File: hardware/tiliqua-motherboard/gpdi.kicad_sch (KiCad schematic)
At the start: 18 parts, among them J10 DVI_GPDI_D_1.4, U3 PCA9306DP

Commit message: big HDMI
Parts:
- J10: footprint Connector_Video:HDMI_Micro-D_Molex_46765-1x01 -> Connector_Video:HDMI_A_Amphenol_10029449-x01xLF_Horizontal
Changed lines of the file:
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@@
 			)
 		)
-		(property "Footprint" "Connector_Video:HDMI_Micro-D_Molex_46765-1x01"
+		(property "Footprint" "Connector_Video:HDMI_A_Amphenol_10029449-x01xLF_Horizontal"
 			(at 172.085 91.44 0)
 			(effects

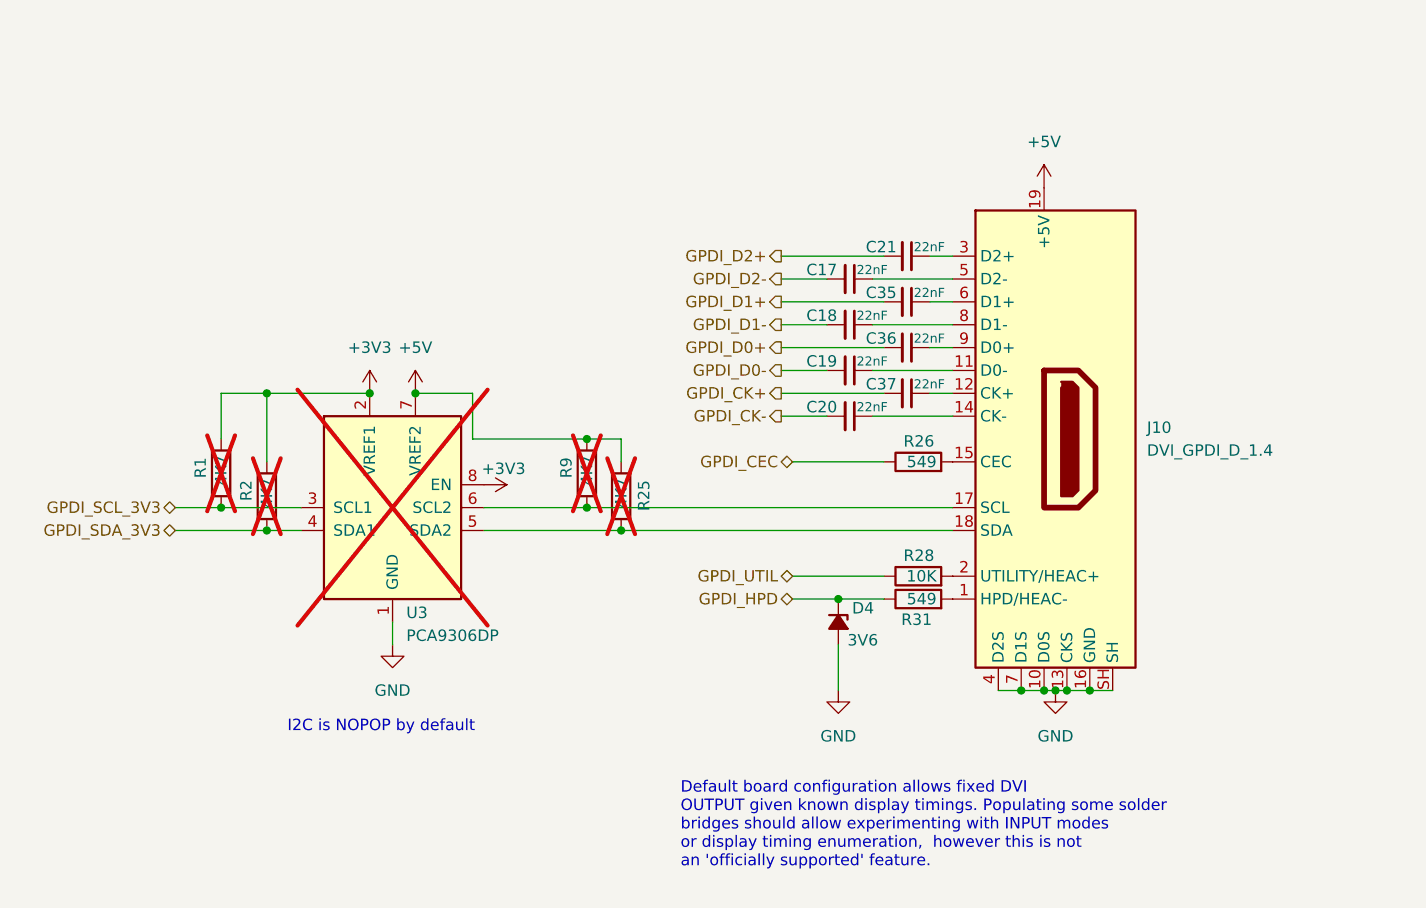
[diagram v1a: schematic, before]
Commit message: schematic cleanup, dual-role usb c
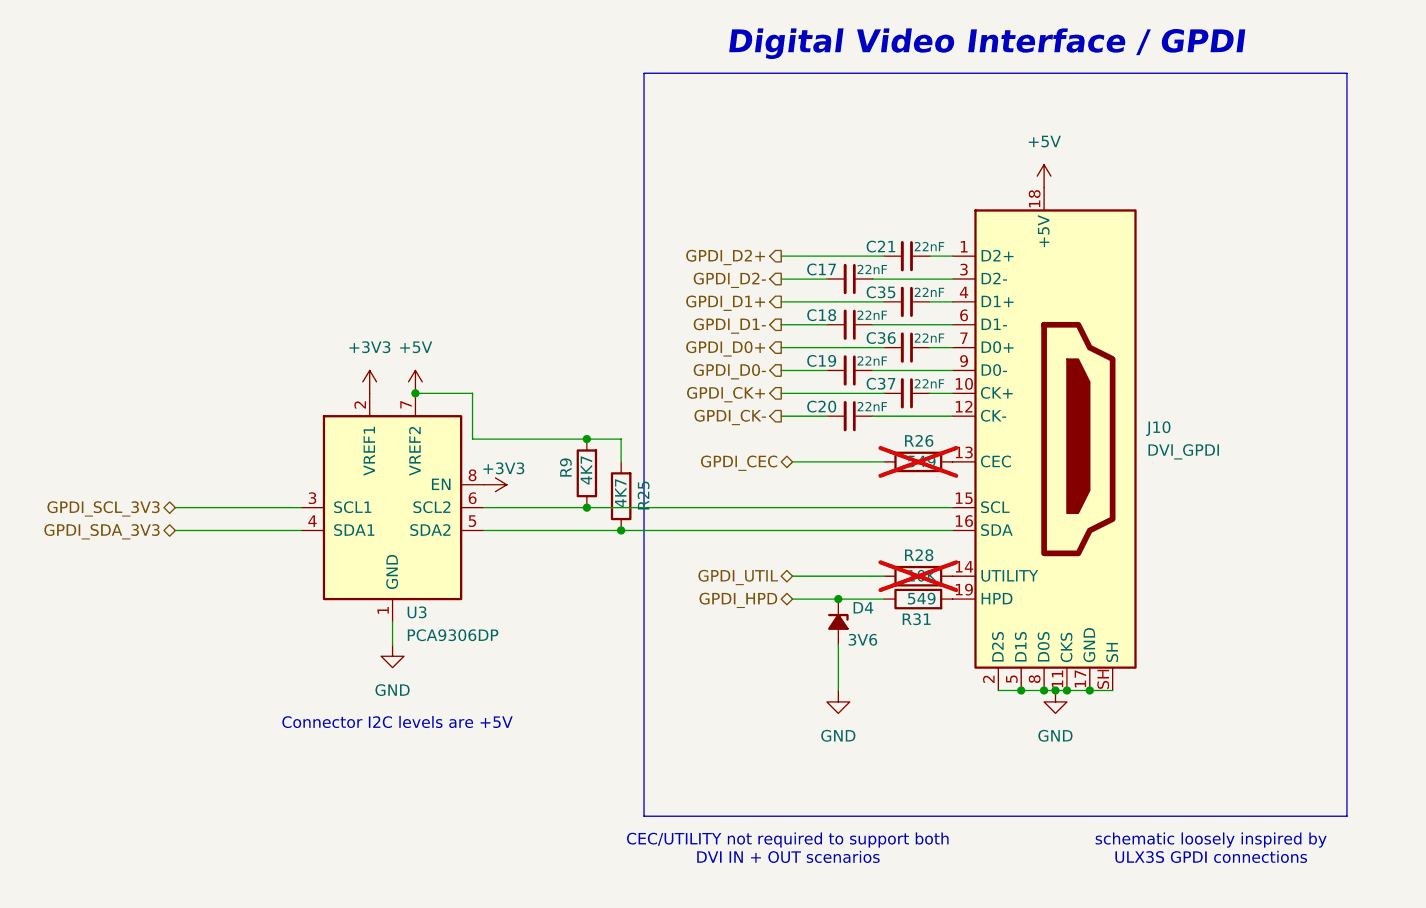
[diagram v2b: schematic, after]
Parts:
- removed J10: DVI_GPDI_D_1.4, Connector_Video:HDMI_A_Amphenol_10029449-x01xLF_Horizontal, symbol Connector:HDMI_D_1.4
- removed R1, R2: 4K7, Resistor_SMD:R_0402_1005Metric, symbol Device:R
- added J10: DVI_GPDI, Connector_Video:HDMI_A_Amphenol_10029449-x01xLF_Horizontal, symbol Connector:HDMI_A
- R25, R9: now fitted
- R26, R28: now not fitted
- U3: footprint Package_SO:SOP-8_3.9x4.9mm_P1.27mm -> Package_SO:TSSOP-8_3x3mm_P0.65mm; lcsc# (none) -> C128835; now fitted
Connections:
- net +5V: now also J10.18 (+5V)
- net GND: now also J10.11 (CKS), J10.17 (GND), J10.2 (D2S), J10.5 (D1S), J10.8 (D0S), J10.SH
- net at C21.1: now also J10.1 (D2+)
- net at C35.1: now also J10.4 (D1+)
- net at R9.1, U3.6 (SCL2): now also J10.15 (SCL)
- net at C20.1: now also J10.12 (CK-)
- net at R25.1, U3.5 (SDA2): now also J10.16 (SDA)
- net at C36.1: now also J10.7 (D0+)
- net at R31.2: now also J10.19 (HPD)
- net at C19.1: now also J10.9 (D0-)
- net at C37.1: now also J10.10 (CK+)
- net at R26.2: now also J10.13 (CEC)
- net at R28.2: now also J10.14 (UTILITY)
- net at C17.1: now also J10.3 (D2-)
- net at C18.1: now also J10.6 (D1-)
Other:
- note added: "CEC/UTILITY not required to support both DVI IN + OUT scenarios"
- note added: "Connector I2C levels are +5V"
- note added: "Digital Video Interface / GPDI"
- note added: "schematic loosely inspired by ULX3S GPDI connections"
- note removed: "Default board configuration allows fixed DVI OUTPUT given known display timings. Populating some solder bridges should allow experimenting with INPUT modes or display timing enumeration, however this is not an 'officially supported' feature."
- note removed: "I2C is NOPOP by default"

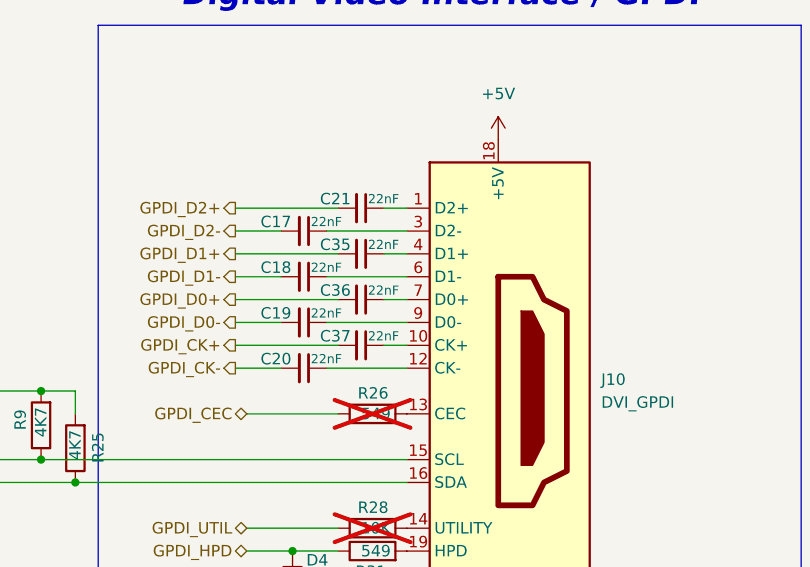
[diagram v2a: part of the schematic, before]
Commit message: fix GPDI diff pairs
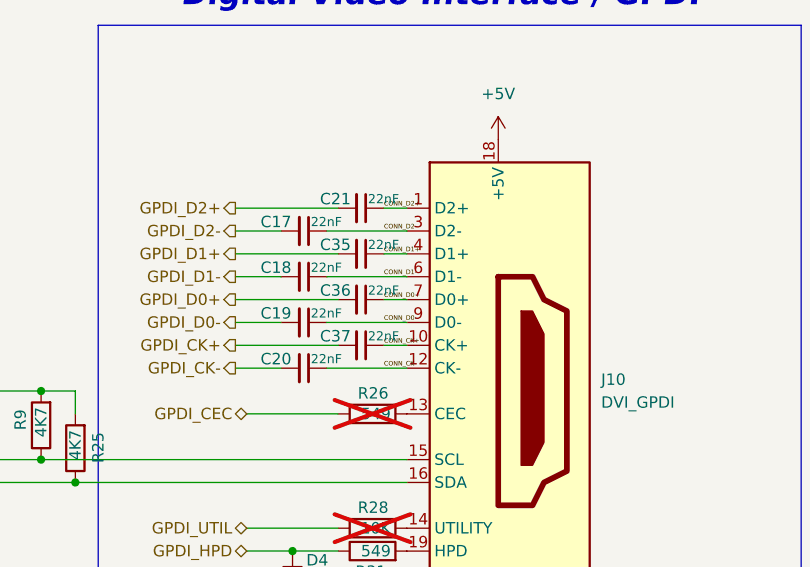
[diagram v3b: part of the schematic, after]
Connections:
- net CONN_D2+: now reaches C21.1, J10.1 (D2+)
- net CONN_D1+: now reaches C35.1, J10.4 (D1+)
- net CONN_CK-: now reaches C20.1, J10.12 (CK-)
- net CONN_D0+: now reaches C36.1, J10.7 (D0+)
- net CONN_CK+: now reaches C37.1, J10.10 (CK+)
- net CONN_D2-: now reaches C17.1, J10.3 (D2-)
- net CONN_D1-: now reaches C18.1, J10.6 (D1-)
- net CONN_D0-: now reaches C19.1, J10.9 (D0-)
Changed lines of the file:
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@@
+		)
+	)
+	(label "CONN_D2+"
+		(at 158.75 71.12 0)
+		(fields_autoplaced yes)
+		(effects
+			(font
+				(size 0.508 0.508)
+			)
+			(justify left bottom)
+		)
+	)
+	(label "CONN_CK-"
+		(at 158.75 88.9 0)
+		(fields_autoplaced yes)
+		(effects
+			(font
+				(size 0.508 0.508)
+			)
+			(justify left bottom)
+		)
+	)
+	(label "CONN_D2-"
+		(at 158.75 73.66 0)
+		(fields_autoplaced yes)
+		(effects
+			(font
+				(size 0.508 0.508)
+			)
+			(justify left bottom)
+		)
+	)
+	(label "CONN_D1-"
+		(at 158.75 78.74 0)
+		(fields_autoplaced yes)
+		(effects
+			(font
+				(size 0.508 0.508)
+			)
+			(justify left bottom)
+		)
+	)
+	(label "CONN_D0+"
+		(at 158.75 81.28 0)
+		(fields_autoplaced yes)
+		(effects
+			(font
+				(size 0.508 0.508)
+			)
+			(justify left bottom)
+		)
+	)
+	(label "CONN_D1+"
+		(at 158.75 76.2 0)
+		(fields_autoplaced yes)
+		(effects
+			(font
+				(size 0.508 0.508)
+			)
+			(justify left bottom)
+		)
+	)
+	(label "CONN_CK+"
+		(at 158.75 86.36 0)
+		(fields_autoplaced yes)
+		(effects
+			(font
+				(size 0.508 0.508)
+			)
+			(justify left bottom)
+		)
+	)
+	(label "CONN_D0-"
+		(at 158.75 83.82 0)
+		(fields_autoplaced yes)
+		(effects
+			(font
+				(size 0.508 0.508)
+			)
+			(justify left bottom)
 		)
 	)

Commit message: button and zener footprints
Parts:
- D4: footprint Diode_SMD:D_SOD-123F -> Diode_SMD:D_SOD-123; lcsc# (none) -> C173412
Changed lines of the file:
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@@
 			)
 		)
-		(property "Footprint" "Diode_SMD:D_SOD-123F"
+		(property "Footprint" "Diode_SMD:D_SOD-123"
 			(at 148.59 111.76 90)
 			(effects
@@
 			(effects
 				(font
+					(size 1.27 1.27)
+				)
+				(hide yes)
+			)
+		)
+		(property "lcsc#" "C173412"
+			(at 148.59 111.76 90)
+			(effects
+				(font

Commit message: add some part numbers
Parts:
- C17, C18, C19, C20, C21, C35, C36, C37: lcsc# (none) -> C1532
- J10: lcsc# (none) -> C428493
- R25, R9: lcsc# (none) -> C25900
- R31: lcsc# (none) -> C474081
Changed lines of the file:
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@@
 			)
 		)
-		(property "lcsc#" ""
+		(property "lcsc#" "C1532"
+			(at 156.21 71.12 0)
+			(effects
+				(font
+					(size 1.27 1.27)
+				)
+				(hide yes)
+			)
+		)
+		(property "Tol" ""
 			(at 156.21 71.12 0)
 			(effects
@@
 			)
 		)
-		(property "lcsc#" ""
+		(property "lcsc#" "C1532"
+			(at 156.21 76.2 0)
+			(effects
+				(font
+					(size 1.27 1.27)
+				)
+				(hide yes)
+			)
+		)
+		(property "Tol" ""
 			(at 156.21 76.2 0)
 			(effects
@@
 			)
 		)
-		(property "lcsc#" ""
+		(property "lcsc#" "C25900"
+			(at 120.65 95.25 0)
+			(effects
+				(font
+					(size 1.27 1.27)
+				)
+				(hide yes)
+			)
+		)
+		(property "Tol" ""
 			(at 120.65 95.25 0)
 			(effects
@@
 			)
 		)
-		(property "lcsc#" ""
+		(property "lcsc#" "C1532"
+			(at 149.86 88.9 0)
+			(effects
+				(font
+					(size 1.27 1.27)
+				)
+				(hide yes)
+			)
+		)
+		(property "Tol" ""
 			(at 149.86 88.9 0)
 			(effects
@@
 			)
 		)
+		(property "Tol" ""
+			(at 99.06 99.06 0)
+			(effects
+				(font
+					(size 1.27 1.27)
+				)
+				(hide yes)
+			)
+		)
 		(pin "8"
 		)
@@
 			)
 		)
-		(property "lcsc#" ""
+		(property "lcsc#" "C1532"
+			(at 156.21 81.28 0)
+			(effects
+				(font
+					(size 1.27 1.27)
+				)
+				(hide yes)
+			)
+		)
+		(property "Tol" ""
 			(at 156.21 81.28 0)
 			(effects
@@
 			)
 		)
+		(property "Tol" ""
+			(at 171.45 91.44 0)
+			(effects
+				(font
+					(size 1.27 1.27)
+				)
+				(hide yes)
+			)
+		)
+		(property "lcsc#" "C428493"
+			(at 171.45 91.44 0)
+			(effects
+				(font
+					(size 1.27 1.27)
+				)
+				(hide yes)
+			)
+		)
 		(pin "14"
 		)
@@
 			)
 		)
+		(property "Tol" ""
+			(at 157.48 106.68 0)
+			(effects
+				(font
+					(size 1.27 1.27)
+				)
+				(hide yes)
+			)
+		)
 		(pin "1"
 		)
@@
 			)
 		)
+		(property "Tol" ""
+			(at 157.48 93.98 0)
+			(effects
+				(font
+					(size 1.27 1.27)
+				)
+				(hide yes)
+			)
+		)
 		(pin "1"
 		)
@@
 			)
 		)
-		(property "lcsc#" ""
+		(property "lcsc#" "C25900"
+			(at 124.46 97.79 0)
+			(effects
+				(font
+					(size 1.27 1.27)
+				)
+				(hide yes)
+			)
+		)
+		(property "Tol" ""
 			(at 124.46 97.79 0)
 			(effects
@@
 			)
 		)
-		(property "lcsc#" ""
+		(property "lcsc#" "C1532"
+			(at 156.21 86.36 0)
+			(effects
+				(font
+					(size 1.27 1.27)
+				)
+				(hide yes)
+			)
+		)
+		(property "Tol" ""
 			(at 156.21 86.36 0)
 			(effects
@@
 			)
 		)
-		(property "lcsc#" ""
+		(property "lcsc#" "C1532"
+			(at 149.86 73.66 0)
+			(effects
+				(font
+					(size 1.27 1.27)
+				)
+				(hide yes)
+			)
+		)
+		(property "Tol" ""
 			(at 149.86 73.66 0)
 			(effects
@@
 			)
 		)
+		(property "Tol" ""
+			(at 148.59 111.76 0)
+			(effects
+				(font
+					(size 1.27 1.27)
+				)
+				(hide yes)
+			)
+		)
 		(pin "2"
 		)
@@
 			)
 		)
-		(property "lcsc#" ""
+		(property "lcsc#" "C474081"
+			(at 157.48 109.22 0)
+			(effects
+				(font
+					(size 1.27 1.27)
+				)
+				(hide yes)
+			)
+		)
+		(property "Tol" ""
 			(at 157.48 109.22 0)
 			(effects
@@
 			)
 		)
-		(property "lcsc#" ""
+		(property "lcsc#" "C1532"
+			(at 149.86 83.82 0)
+			(effects
+				(font
+					(size 1.27 1.27)
+				)
+				(hide yes)
+			)
+		)
+		(property "Tol" ""
 			(at 149.86 83.82 0)
 			(effects
@@
 			)
 		)
-		(property "lcsc#" ""
+		(property "lcsc#" "C1532"
 			(at 149.86 78.74 0)
 			(effects
+				(font
+					(size 1.27 1.27)
+				)
+				(hide yes)
+			)
+		)
+		(property "Tol" ""
+			(at 149.86 78.74 0)
+			(effects

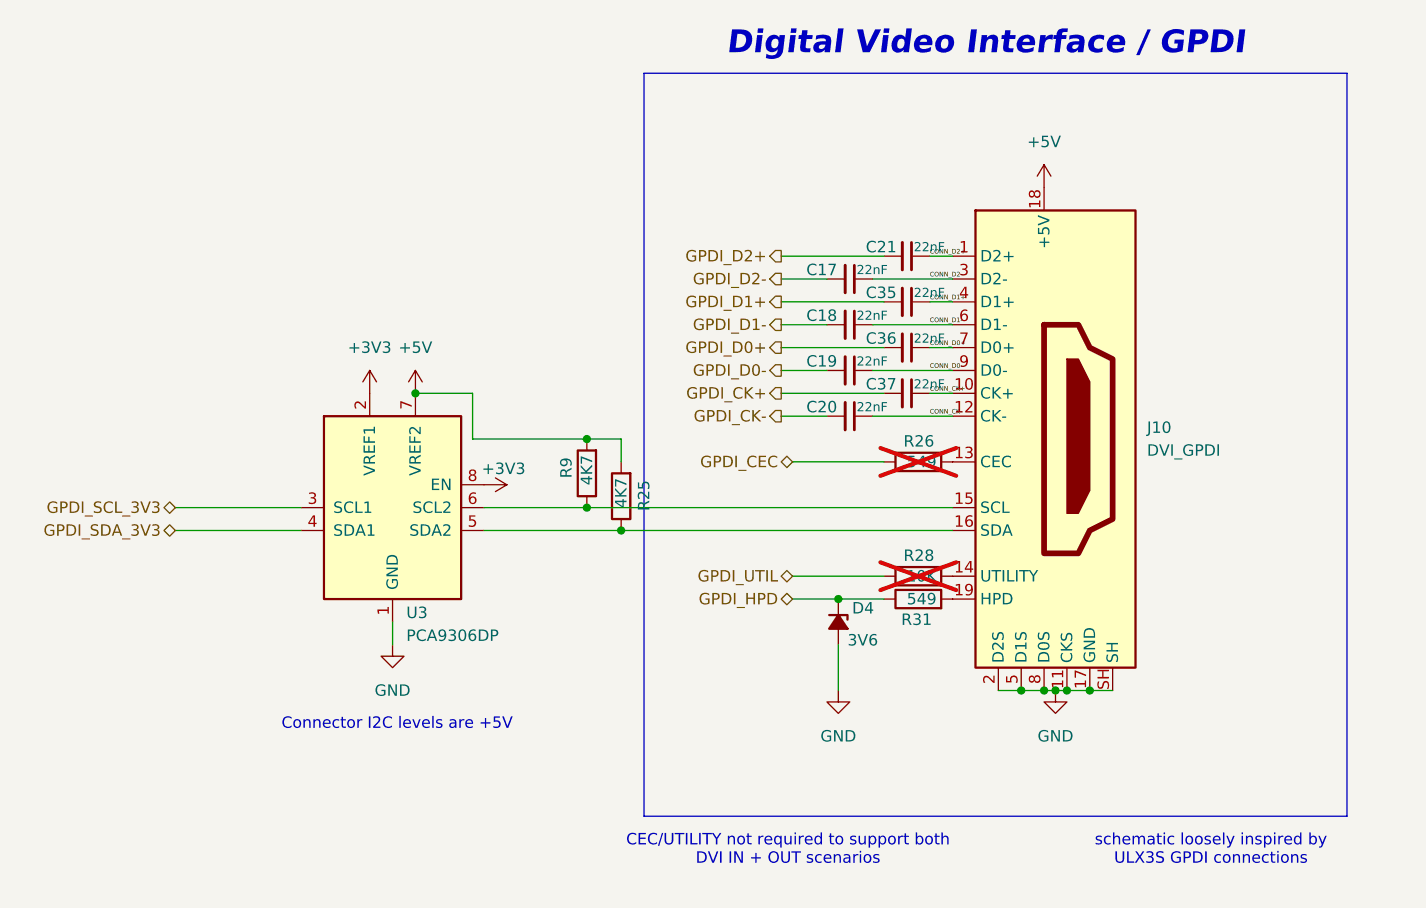
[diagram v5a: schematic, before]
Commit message: more sane DVI PHY
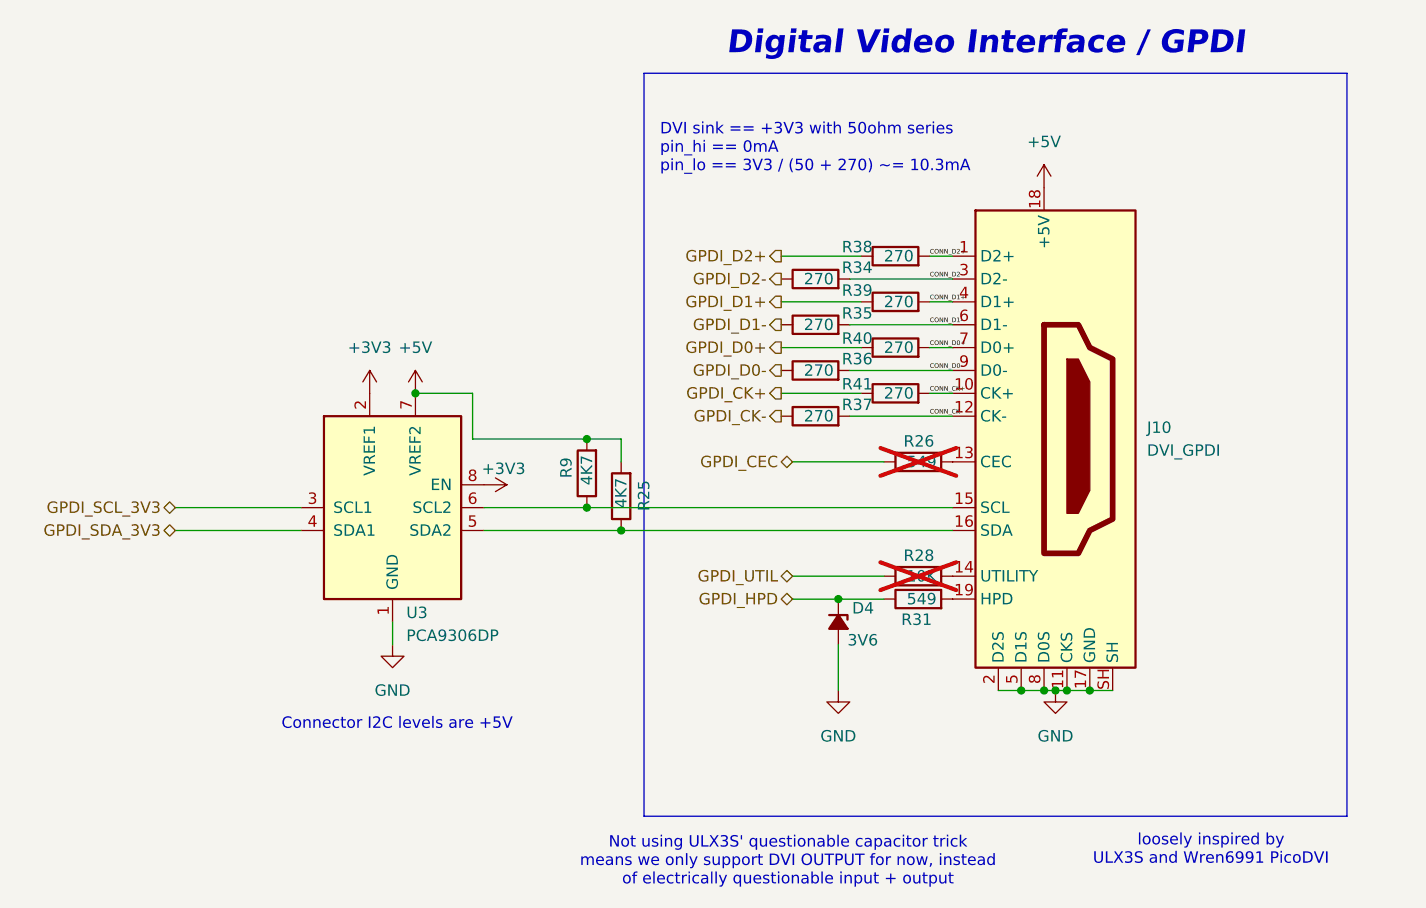
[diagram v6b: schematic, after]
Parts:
- removed C17, C18, C19, C20, C21, C35, C36, C37: 22nF, Capacitor_SMD:C_0402_1005Metric, symbol OLIMEX_RCL:C
- added R34, R35, R36, R37, R38, R39, R40, R41: 270, Resistor_SMD:R_0402_1005Metric, symbol Device:R
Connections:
- net CONN_CK+: now also R41.2
- net CONN_CK-: now also R37.2
- net CONN_D0+: now also R40.2
- net CONN_D0-: now also R36.2
- net CONN_D1+: now also R39.2
- net CONN_D1-: now also R35.2
- net CONN_D2+: now also R38.2
- net CONN_D2-: now also R34.2
- net GPDI_CK+: now also R41.1
- net GPDI_CK-: now also R37.1
- net GPDI_D0+: now also R40.1
- net GPDI_D0-: now also R36.1
- net GPDI_D1+: now also R39.1
- net GPDI_D1-: now also R35.1
- net GPDI_D2+: now also R38.1
- net GPDI_D2-: now also R34.1
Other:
- note added: "DVI sink == +3V3 with 50ohm series pin_hi == 0mA pin_lo == 3V3 / (50 + 270) ~= 10.3mA"
- note added: "Not using ULX3S' questionable capacitor trick means we only support DVI OUTPUT for now, instead of electrically questionable input + output"
- note added: "loosely inspired by ULX3S and Wren6991 PicoDVI"
- note removed: "CEC/UTILITY not required to support both DVI IN + OUT scenarios"
- note removed: "schematic loosely inspired by ULX3S GPDI connections"

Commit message: hw/mobo-r3: +5V I2C bridge fix + EN, +12V ingress 200mA->350mA fuse, GPDI +5V NONE->50mA fuse
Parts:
- added F3: 15V 50mA, Fuse:Fuse_0805_2012Metric, symbol Device:Polyfuse_Small
- added R44: 200K, Resistor_SMD:R_0402_1005Metric, symbol Device:R
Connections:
- net +3V3: no longer U3.8 (EN)
- net +5V: now also F3.2, R44.1; no longer J10.18 (+5V), U3.7 (VREF2)
- new net: R44.2, U3.7 (VREF2)
- new net: F3.1, J10.18 (+5V)
- new net I2C_EN: U3.8 (EN)
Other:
- moved on the sheet: R9

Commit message: hw/mobo-r3: remove +5V EN (incorrect), clean DRC
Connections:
- net I2C_EN is gone; now on an unnamed net: U3.8 (EN)
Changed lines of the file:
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@@
+	)
+	(junction
+		(at 109.22 86.36)
+		(diameter 0)
+		(color 0 0 0 0)
 	)
 	(junction
@@
 	(wire
 		(pts
+			(xy 109.22 86.36) (xy 110.49 86.36)
+		)
+		(stroke
+			(width 0)
+			(type default)
+		)
+	)
+	(wire
+		(pts
 			(xy 142.24 81.28) (xy 151.13 81.28)
 		)
@@
 	(wire
 		(pts
-			(xy 101.6 86.36) (xy 110.49 86.36)
+			(xy 109.22 86.36) (xy 109.22 96.52)
+		)
+		(stroke
+			(width 0)
+			(type default)
+		)
+	)
+	(wire
+		(pts
+			(xy 101.6 86.36) (xy 109.22 86.36)
 		)
 		(stroke
@@
 		)
 	)
-	(hierarchical_label "I2C_EN"
-		(shape bidirectional)
-		(at 109.22 96.52 0)
-		(fields_autoplaced yes)
-		(effects
-			(font
-				(size 1.27 1.27)
-			)
-			(justify left)
-		)
-	)
